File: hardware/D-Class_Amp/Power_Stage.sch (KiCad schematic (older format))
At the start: 22 parts, among them Q501 PHP23NQ11T, Q502 PHP23NQ11T, Q503 PHP23NQ11T, Q504 PHP23NQ11T, U502 IR21834, U503 IR21834

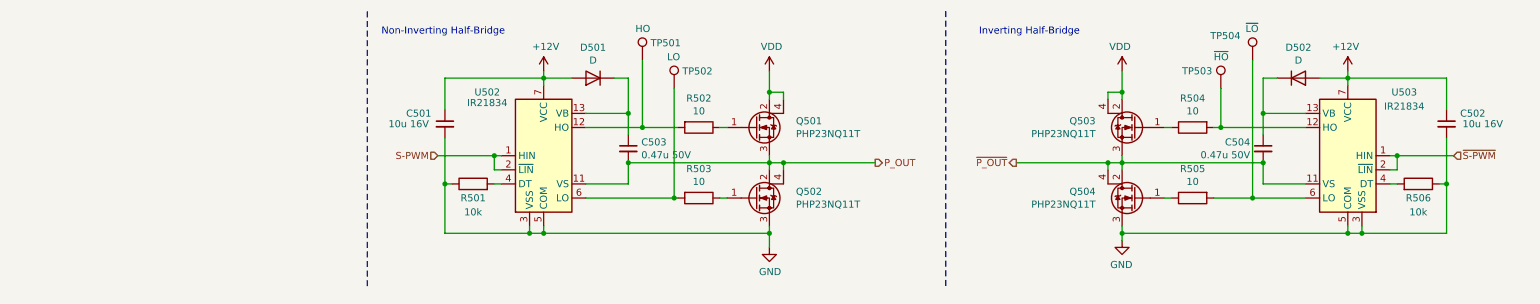
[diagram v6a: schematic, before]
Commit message: added pricing and and part numbers to all components
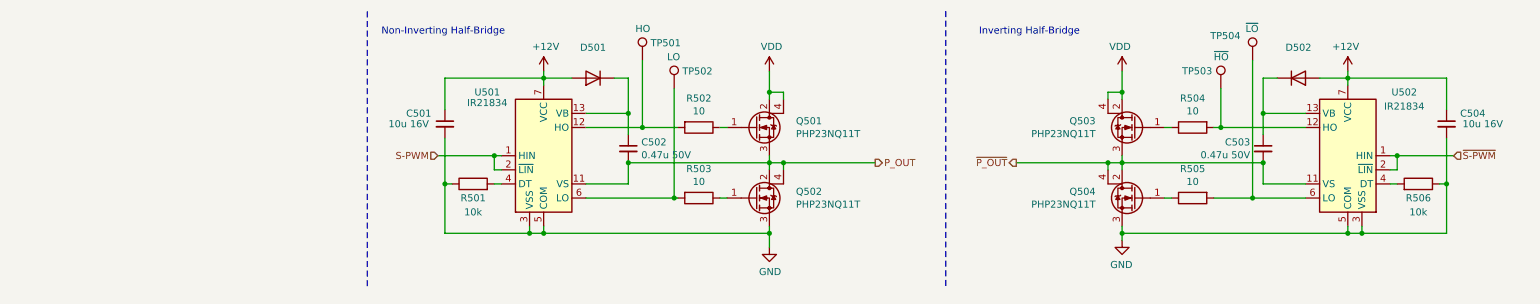
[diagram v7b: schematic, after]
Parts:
- C501: DigiKey Price (none) -> 0.34; Part Number (none) -> CL21A106KOQNNWE
- C502: renamed from C503; DigiKey Price (none) -> 0.16; Part Number (none) -> CL21B474KBFNNNG
- C503: renamed from C504; DigiKey Price (none) -> 0.16; Part Number (none) -> CL21B474KBFNNNG
- C504: renamed from C502; DigiKey Price (none) -> 0.34; Part Number (none) -> CL21A106KOQNNWE
- D501, D502: value D -> UG1B-E3/54; footprint (none) -> Diode_THT:D_DO-41_SOD81_P7.62mm_Horizontal; DigiKey Price (none) -> 0.77; Part Number (none) -> UG1B-E3/54
- R501, R506: DigiKey Price (none) -> 0.16; Part Number (none) -> RC0805JR-0710KL
- R502, R503, R504, R505: DigiKey Price (none) -> 0.16; Part Number (none) -> ERJ-6ENF10R0V
- U501: renamed from U502; DigiKey Price (none) -> 5.87
- U502: renamed from U503; DigiKey Price (none) -> 5.87
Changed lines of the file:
@@
 $EndDescr
 $Comp
-L power:VDD #PWR0505
+L power:VDD #PWR0502
 U 1 1 6105D8A1
 P 5850 900
-F 0 "#PWR0505" H 5850 750 50  0001 C CNN
+F 0 "#PWR0502" H 5850 750 50  0001 C CNN
 F 1 "VDD" H 5865 1073 50  0000 C CNN
 F 2 "" H 5850 900 50  0001 C CNN
@@
 S-PWM
 $Comp
-L Device:C_Small C503
+L Device:C_Small C502
 U 1 1 610A4CCB
 P 4850 1450
-F 0 "C503" H 4942 1496 50  0000 L CNN
+F 0 "C502" H 4942 1496 50  0000 L CNN
 F 1 "0.47u 50V" H 4942 1405 50  0000 L CNN
 F 2 "Capacitor_SMD:C_0805_2012Metric_Pad1.18x1.45mm_HandSolder" H 4850 1450 50  0001 C CNN
 F 3 "~" H 4850 1450 50  0001 C CNN
+F 4 "0.16" H 4850 1450 50  0001 C CNN "DigiKey Price"
+F 5 "CL21B474KBFNNNG" H 4850 1450 50  0001 C CNN "Part Number"
 	1    4850 1450
 	1    0    0    -1
 $EndComp
 $Comp
-L power:+12V #PWR0504
+L power:+12V #PWR0501
 U 1 1 610ABD74
 P 4250 900
-F 0 "#PWR0504" H 4250 750 50  0001 C CNN
+F 0 "#PWR0501" H 4250 750 50  0001 C CNN
 F 1 "+12V" H 4265 1073 50  0000 C CNN
 F 2 "" H 4250 900 50  0001 C CNN
@@
 P 4600 950
 F 0 "D501" H 4600 733 50  0000 C CNN
-F 1 "D" H 4600 824 50  0000 C CNN
-F 2 "" H 4600 950 50  0001 C CNN
-F 3 "~" H 4600 950 50  0001 C CNN
+F 1 "UG1B-E3/54" H 4600 824 50  0000 C CNN
+F 2 "Diode_THT:D_DO-41_SOD81_P7.62mm_Horizontal" H 4600 950 50  0001 C CNN
+F 3 "~https://media.digikey.com/pdf/Data%20Sheets/Vishay%20Semiconductors/UG1A-UG1D.pdf" H 4600 950 50  0001 C CNN
+F 4 "0.77" H 4600 950 50  0001 C CNN "DigiKey Price"
+F 5 "UG1B-E3/54" H 4600 950 50  0001 C CNN "Part Number"
 	1    4600 950
 	-1   0    0    1
@@
 F 2 "Resistor_SMD:R_0805_2012Metric_Pad1.20x1.40mm_HandSolder" V 3680 1700 50  0001 C CNN
 F 3 "~" H 3750 1700 50  0001 C CNN
+F 4 "0.16" H 3750 1700 50  0001 C CNN "DigiKey Price"
+F 5 "RC0805JR-0710KL" H 3750 1700 50  0001 C CNN "Part Number"
 	1    3750 1700
 	0    -1   -1   0
@@
 $EndComp
 $Comp
-L Driver_FET:IR21834 U502
+L Driver_FET:IR21834 U501
 U 1 1 6104C522
 P 4250 1500
-F 0 "U502" H 3850 1950 50  0000 C CNN
+F 0 "U501" H 3850 1950 50  0000 C CNN
 F 1 "IR21834" H 3850 1875 50  0000 C CNN
 F 2 "Package_SO:SOIC-14_3.9x8.7mm_P1.27mm" H 4250 1500 50  0001 C CIN
 F 3 "https://www.infineon.com/dgdl/ir2183.pdf?fileId=5546d462533600a4015355c9490e16d1" H 4250 1500 50  0001 C CNN
 F 4 "IR21834SPBFDKR-ND" H 4250 1500 50  0001 C CNN "Part Number"
+F 5 "5.87" H 4250 1500 50  0001 C CNN "DigiKey Price"
 	1    4250 1500
 	1    0    0    -1
 $EndComp
 $Comp
-L power:GND #PWR0506
+L power:GND #PWR0503
 U 1 1 6107E9DB
 P 5850 2150
-F 0 "#PWR0506" H 5850 1900 50  0001 C CNN
+F 0 "#PWR0503" H 5850 1900 50  0001 C CNN
 F 1 "GND" H 5855 1977 50  0000 C CNN
 F 2 "" H 5850 2150 50  0001 C CNN
@@
 	5850 2050 5850 2150
 $Comp
-L power:GND #PWR0508
+L power:GND #PWR0505
 U 1 1 610A1CEE
 P 8350 2100
-F 0 "#PWR0508" H 8350 1850 50  0001 C CNN
+F 0 "#PWR0505" H 8350 1850 50  0001 C CNN
 F 1 "GND" H 8355 1927 50  0000 C CNN
 F 2 "" H 8350 2100 50  0001 C CNN
@@
 $EndComp
 $Comp
-L Driver_FET:IR21834 U503
+L Driver_FET:IR21834 U502
 U 1 1 610F2212
 P 9950 1500
-F 0 "U503" H 9550 1950 50  0000 C CNN
+F 0 "U502" H 9550 1950 50  0000 C CNN
 F 1 "IR21834" H 9550 1850 50  0000 C CNN
 F 2 "Package_SO:SOIC-14_3.9x8.7mm_P1.27mm" H 9950 1500 50  0001 C CIN
 F 3 "https://www.infineon.com/dgdl/ir2183.pdf?fileId=5546d462533600a4015355c9490e16d1" H 9950 1500 50  0001 C CNN
 F 4 "IR21834SPBFDKR-ND" H 9950 1500 50  0001 C CNN "Part Number"
+F 5 "5.87" H 9950 1500 50  0001 C CNN "DigiKey Price"
 	1    9950 1500
 	-1   0    0    -1
@@
 F 1 "10" V 8734 1300 50  0000 C CNN
 F 2 "Resistor_SMD:R_0805_2012Metric_Pad1.20x1.40mm_HandSolder" V 8780 1300 50  0001 C CNN
-F 3 "~" H 8850 1300 50  0001 C CNN
+F 3 "https://industrial.panasonic.com/cdbs/www-data/pdf/RDA0000/AOA0000C304.pdf" H 8850 1300 50  0001 C CNN
+F 4 "0.16" H 8850 1300 50  0001 C CNN "DigiKey Price"
+F 5 "ERJ-6ENF10R0V" H 8850 1300 50  0001 C CNN "Part Number"
 	1    8850 1300
 	0    -1   1    0
@@
 P 9600 950
 F 0 "D502" H 9600 733 50  0000 C CNN
-F 1 "D" H 9600 824 50  0000 C CNN
-F 2 "" H 9600 950 50  0001 C CNN
-F 3 "~" H 9600 950 50  0001 C CNN
+F 1 "UG1B-E3/54" H 9600 824 50  0000 C CNN
+F 2 "Diode_THT:D_DO-41_SOD81_P7.62mm_Horizontal" H 9600 950 50  0001 C CNN
+F 3 "~https://media.digikey.com/pdf/Data%20Sheets/Vishay%20Semiconductors/UG1A-UG1D.pdf" H 9600 950 50  0001 C CNN
+F 4 "0.77" H 9600 950 50  0001 C CNN "DigiKey Price"
+F 5 "UG1B-E3/54" H 9600 950 50  0001 C CNN "Part Number"
 	1    9600 950
 	1    0    0    1
@@
 	10700 1500 10300 1500
 $Comp
-L power:+12V #PWR0509
+L power:+12V #PWR0506
 U 1 1 610F2278
 P 9950 900
-F 0 "#PWR0509" H 9950 750 50  0001 C CNN
+F 0 "#PWR0506" H 9950 750 50  0001 C CNN
 F 1 "+12V" H 9965 1073 50  0000 C CNN
 F 2 "" H 9950 900 50  0001 C CNN
@@
 $EndComp
 $Comp
-L Device:C_Small C504
+L Device:C_Small C503
 U 1 1 610F226E
 P 9350 1450
-F 0 "C504" H 9442 1496 50  0000 L CNN
+F 0 "C503" H 9442 1496 50  0000 L CNN
 F 1 "0.47u 50V" H 9442 1405 50  0000 L CNN
 F 2 "Capacitor_SMD:C_0805_2012Metric_Pad1.18x1.45mm_HandSolder" H 9350 1450 50  0001 C CNN
 F 3 "~" H 9350 1450 50  0001 C CNN
+F 4 "0.16" H 9350 1450 50  0001 C CNN "DigiKey Price"
+F 5 "CL21B474KBFNNNG" H 9350 1450 50  0001 C CNN "Part Number"
 	1    9350 1450
 	-1   0    0    -1
 $EndComp
 $Comp
-L power:VDD #PWR0507
+L power:VDD #PWR0504
 U 1 1 610F224E
 P 8350 900
-F 0 "#PWR0507" H 8350 750 50  0001 C CNN
+F 0 "#PWR0504" H 8350 750 50  0001 C CNN
 F 1 "VDD" H 8365 1073 50  0000 C CNN
 F 2 "" H 8350 900 50  0001 C CNN
@@
 F 2 "Resistor_SMD:R_0805_2012Metric_Pad1.20x1.40mm_HandSolder" V 10380 1700 50  0001 C CNN
 F 3 "~" H 10450 1700 50  0001 C CNN
+F 4 "0.16" H 10450 1700 50  0001 C CNN "DigiKey Price"
+F 5 "RC0805JR-0710KL" H 10450 1700 50  0001 C CNN "Part Number"
 	1    10450 1700
 	0    1    -1   0
@@
 F 1 "10" V 8734 1800 50  0000 C CNN
 F 2 "Resistor_SMD:R_0805_2012Metric_Pad1.20x1.40mm_HandSolder" V 8780 1800 50  0001 C CNN
-F 3 "~" H 8850 1800 50  0001 C CNN
+F 3 "https://industrial.panasonic.com/cdbs/www-data/pdf/RDA0000/AOA0000C304.pdf" H 8850 1800 50  0001 C CNN
+F 4 "0.16" H 8850 1800 50  0001 C CNN "DigiKey Price"
+F 5 "ERJ-6ENF10R0V" H 8850 1800 50  0001 C CNN "Part Number"
 	1    8850 1800
 	0    -1   1    0
@@
 F 1 "10" V 5234 1800 50  0000 C CNN
 F 2 "Resistor_SMD:R_0805_2012Metric_Pad1.20x1.40mm_HandSolder" V 5280 1800 50  0001 C CNN
-F 3 "~" H 5350 1800 50  0001 C CNN
+F 3 "https://industrial.panasonic.com/cdbs/www-data/pdf/RDA0000/AOA0000C304.pdf" H 5350 1800 50  0001 C CNN
+F 4 "0.16" H 5350 1800 50  0001 C CNN "DigiKey Price"
+F 5 "ERJ-6ENF10R0V" H 5350 1800 50  0001 C CNN "Part Number"
 	1    5350 1800
 	0    1    1    0
@@
 F 1 "10" V 5234 1300 50  0000 C CNN
 F 2 "Resistor_SMD:R_0805_2012Metric_Pad1.20x1.40mm_HandSolder" V 5280 1300 50  0001 C CNN
-F 3 "~" H 5350 1300 50  0001 C CNN
+F 3 "https://industrial.panasonic.com/cdbs/www-data/pdf/RDA0000/AOA0000C304.pdf" H 5350 1300 50  0001 C CNN
+F 4 "0.16" H 5350 1300 50  0001 C CNN "DigiKey Price"
+F 5 "ERJ-6ENF10R0V" H 5350 1300 50  0001 C CNN "Part Number"
 	1    5350 1300
 	0    1    1    0
@@
 F 2 "Capacitor_SMD:C_0805_2012Metric_Pad1.18x1.45mm_HandSolder" H 3550 1275 50  0001 C CNN
 F 3 "~" H 3550 1275 50  0001 C CNN
+F 4 "0.34" H 3550 1275 50  0001 C CNN "DigiKey Price"
+F 5 "CL21A106KOQNNWE" H 3550 1275 50  0001 C CNN "Part Number"
 	1    3550 1275
 	1    0    0    -1
 $EndComp
 $Comp
-L Device:C_Small C502
+L Device:C_Small C504
 U 1 1 6119B46C
 P 10650 1275
-F 0 "C502" H 10375 1350 50  0000 L CNN
+F 0 "C504" H 10375 1350 50  0000 L CNN
 F 1 "10u 16V" H 10250 1275 50  0000 L CNN
 F 2 "Capacitor_SMD:C_0805_2012Metric_Pad1.18x1.45mm_HandSolder" H 10650 1275 50  0001 C CNN
 F 3 "~" H 10650 1275 50  0001 C CNN
+F 4 "0.34" H 10650 1275 50  0001 C CNN "DigiKey Price"
+F 5 "CL21A106KOQNNWE" H 10650 1275 50  0001 C CNN "Part Number"
 	1    10650 1275
 	-1   0    0    -1

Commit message: updated the BOM
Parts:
- Q501, Q502, Q503, Q504: DigiKey Price (none) -> 1.90; Part Number (none) -> PHP23NQ11T,127
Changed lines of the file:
@@
 F 2 "Package_TO_SOT_THT:TO-251-3-1EP_Horizontal_TabDown" H 5950 1400 50  0001 C CNN
 F 3 "https://assets.nexperia.com/documents/data-sheet/PHP23NQ11T.pdf" H 5750 1300 50  0001 C CNN
+F 4 "1.90" H 5750 1300 50  0001 C CNN "DigiKey Price"
+F 5 "PHP23NQ11T,127" H 5750 1300 50  0001 C CNN "Part Number"
 	1    5750 1300
 	1    0    0    -1
@@
 F 2 "Package_TO_SOT_THT:TO-251-3-1EP_Horizontal_TabDown" H 5950 1900 50  0001 C CNN
 F 3 "https://assets.nexperia.com/documents/data-sheet/PHP23NQ11T.pdf" H 5750 1800 50  0001 C CNN
+F 4 "1.90" H 5750 1800 50  0001 C CNN "DigiKey Price"
+F 5 "PHP23NQ11T,127" H 5750 1800 50  0001 C CNN "Part Number"
 	1    5750 1800
 	1    0    0    -1
@@
 F 2 "Package_TO_SOT_THT:TO-251-3-1EP_Horizontal_TabDown" H 8650 1400 50  0001 C CNN
 F 3 "https://assets.nexperia.com/documents/data-sheet/PHP23NQ11T.pdf" H 8450 1300 50  0001 C CNN
+F 4 "1.90" H 8450 1300 50  0001 C CNN "DigiKey Price"
+F 5 "PHP23NQ11T,127" H 8450 1300 50  0001 C CNN "Part Number"
 	1    8450 1300
 	-1   0    0    -1
@@
 F 2 "Package_TO_SOT_THT:TO-251-3-1EP_Horizontal_TabDown" H 8650 1900 50  0001 C CNN
 F 3 "https://assets.nexperia.com/documents/data-sheet/PHP23NQ11T.pdf" H 8450 1800 50  0001 C CNN
+F 4 "1.90" H 8450 1800 50  0001 C CNN "DigiKey Price"
+F 5 "PHP23NQ11T,127" H 8450 1800 50  0001 C CNN "Part Number"
 	1    8450 1800
 	-1   0    0    -1
